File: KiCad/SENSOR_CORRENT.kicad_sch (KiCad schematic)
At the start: 0 parts

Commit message: Actualització del sensor de corrent
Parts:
- added C1: C, symbol Device:C
- added R1: R, symbol Device:R
- added R_Shunt: 10m, symbol Device:R_Shunt
- added U2: INA180A1, Package_TO_SOT_SMD:SOT-23-5, symbol Amplifier_Current:INA180A1
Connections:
- new net: R1.2, U2.1
- new net GND: C1.2, R_Shunt.4, U2.2 (GND)
- new net MOTOR_SENSE_IN: R_Shunt.1
- new net SHUNT_HIGH: R_Shunt.2, U2.3 (+)
- new net SHUNT_LOW: R_Shunt.3, U2.4 (-)
- new net VDD_3V3: U2.5 (V+)
- new net WIN_CURRENT_ADC: C1.1, R1.1

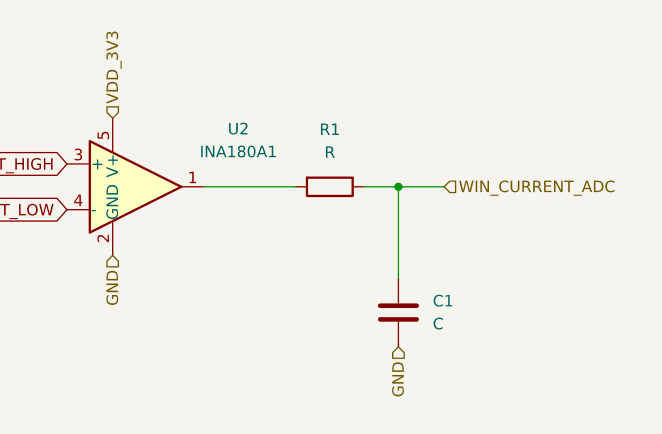
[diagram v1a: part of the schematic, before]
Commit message: Versió amb el simbol del nou micro
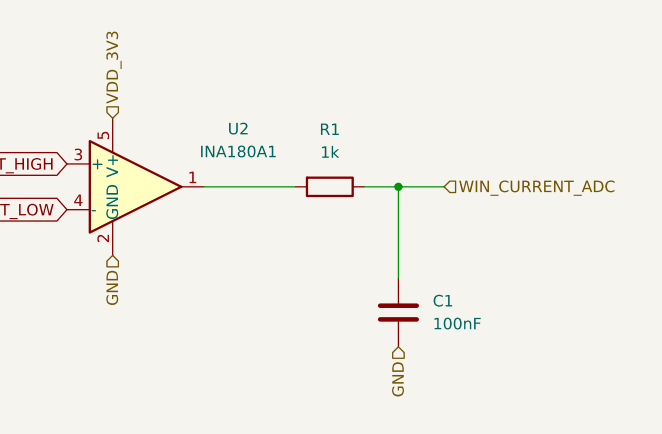
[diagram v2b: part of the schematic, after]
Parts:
- C1: value C -> 100nF
- R1: value R -> 1k
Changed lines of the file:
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@@
 		)
 		(instances
+			(project "SENSOR_CORRENT"
+				(path "/03eea87e-da87-4f21-8136-ad0584e7714c"
+					(reference "R_Shunt1")
+					(unit 1)
+				)
+			)
 			(project ""
 				(path "/347831db-5db9-4aff-ad32-e56fd770e219/0aa311db-868d-4102-819d-96f0255ccb92"
@@
 			)
 		)
-		(property "Value" "R"
+		(property "Value" "1k"
 			(at 132.08 38.1 90)
 			(effects
@@
 		)
 		(instances
+			(project "SENSOR_CORRENT"
+				(path "/03eea87e-da87-4f21-8136-ad0584e7714c"
+					(reference "R1")
+					(unit 1)
+				)
+			)
 			(project ""
 				(path "/347831db-5db9-4aff-ad32-e56fd770e219/0aa311db-868d-4102-819d-96f0255ccb92"
@@
 		)
 		(instances
+			(project "SENSOR_CORRENT"
+				(path "/03eea87e-da87-4f21-8136-ad0584e7714c"
+					(reference "U1")
+					(unit 1)
+				)
+			)
 			(project ""
 				(path "/347831db-5db9-4aff-ad32-e56fd770e219/0aa311db-868d-4102-819d-96f0255ccb92"
@@
 			)
 		)
-		(property "Value" "C"
+		(property "Value" "100nF"
 			(at 143.51 57.1499 0)
 			(effects
@@
 		)
 		(instances
-			(project ""
-				(path "/347831db-5db9-4aff-ad32-e56fd770e219/0aa311db-868d-4102-819d-96f0255ccb92"
+			(project "SENSOR_CORRENT"
+				(path "/03eea87e-da87-4f21-8136-ad0584e7714c"
 					(reference "C1")
 					(unit 1)
 				)
 			)
-		)
-	)
+			(project ""
+				(path "/347831db-5db9-4aff-ad32-e56fd770e219/0aa311db-868d-4102-819d-96f0255ccb92"
+					(reference "C1")
+					(unit 1)
+				)
+			)
+		)
+	)
+	(sheet_instances
+		(path "/"
+			(page "1")
+		)
+	)
+	(embedded_fonts no)
 )

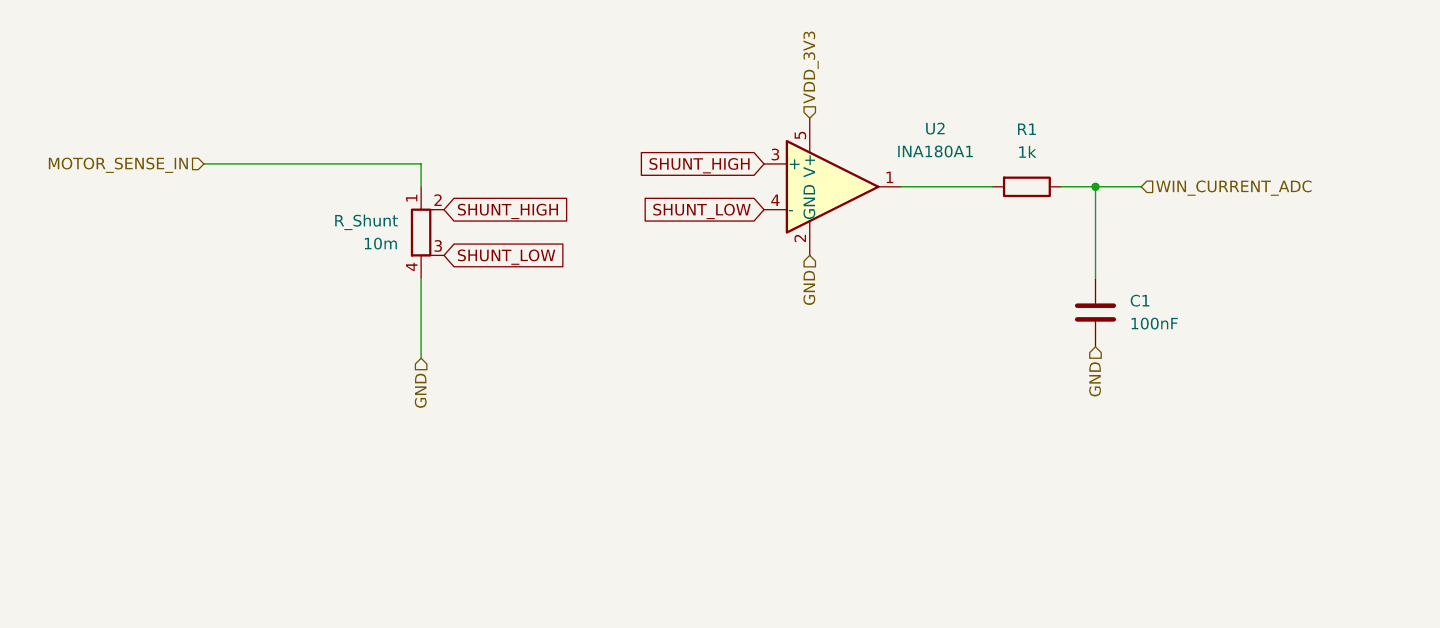
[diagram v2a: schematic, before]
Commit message: Footprints afegides a Comunicació, Sensor RFID i Sensor Corrent
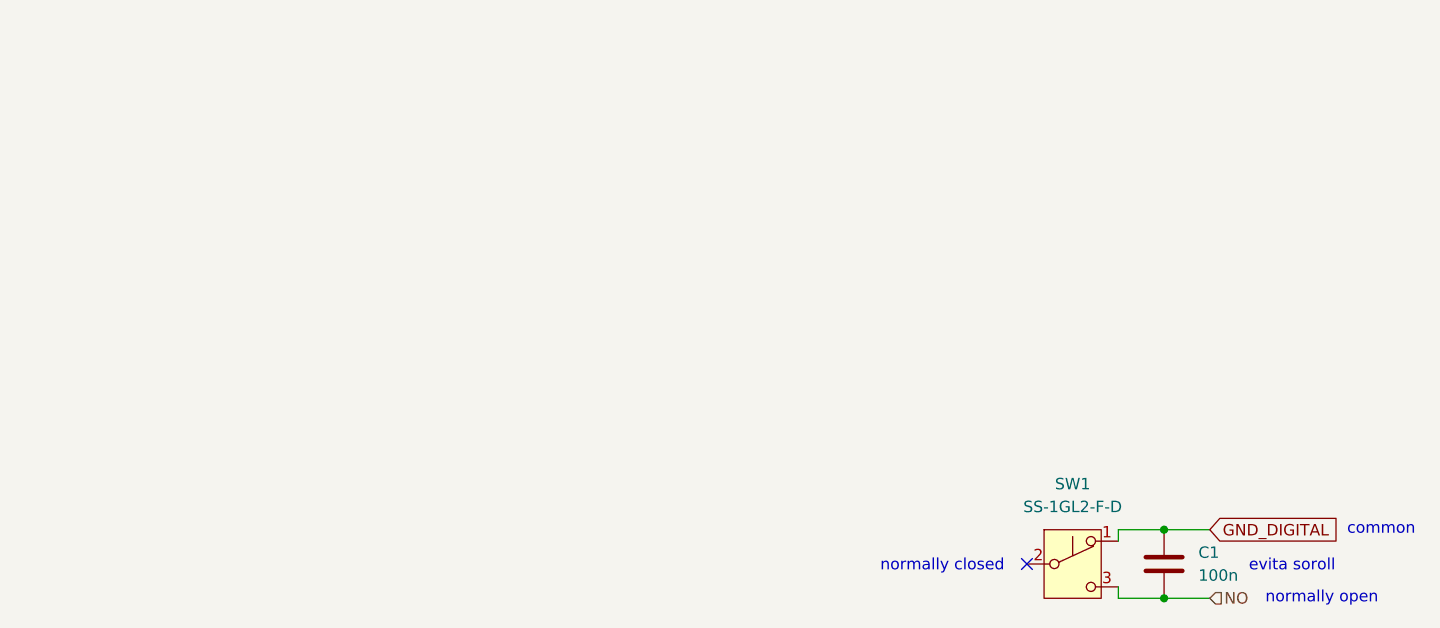
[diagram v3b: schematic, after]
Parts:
- removed R1: 1k, symbol Device:R
- removed R_Shunt: 10m, symbol Device:R_Shunt
- removed U2: INA180A1, Package_TO_SOT_SMD:SOT-23-5, symbol Amplifier_Current:INA180A1
- added SW1: SS-1GL2-F-D, symbol Switch:SW_Push_SPDT
- C1: value 100nF -> 100n; footprint (none) -> Capacitor_SMD:C_0805_2012Metric_Pad1.18x1.45mm_HandSolder
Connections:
- net GND renamed NO
- net NO: now also SW1.3 (NO)
- net WIN_CURRENT_ADC renamed GND_DIGITAL
- net GND_DIGITAL: now also SW1.1 (COM)
- no-connect marks 0 -> 1
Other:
- note added: "common"
- note added: "evita soroll"
- note added: "normally closed"
- note added: "normally open"

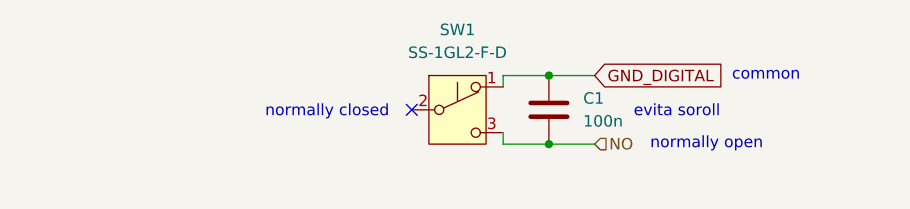
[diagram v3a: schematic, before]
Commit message: Nova versió diagrama de blocs + BOM actualitzat + Nova versió KiCad
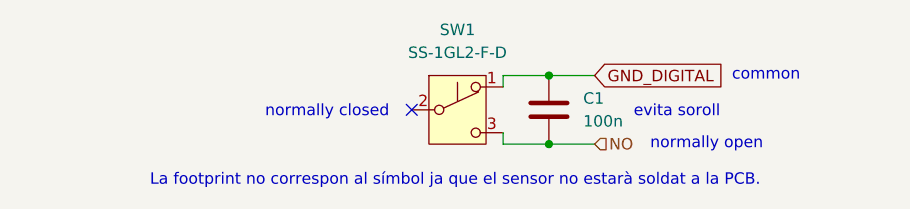
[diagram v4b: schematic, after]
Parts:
- SW1: footprint (none) -> Connector_PinSocket_1.00mm:PinSocket_1x03_P1.00mm_Vertical
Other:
- note added: "La footprint no correspon al símbol ja que el sensor no estarà soldat a la PCB."
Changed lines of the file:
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@@
+		)
+	)
+	(text "La footprint no correspon al símbol ja que el sensor no estarà soldat a la PCB."
+		(exclude_from_sim no)
+		(at 136.906 91.694 0)
+		(effects
+			(font
+				(size 1.27 1.27)
+			)
 		)
 	)
@@
 			)
 		)
-		(property "Footprint" ""
+		(property "Footprint" "Connector_PinSocket_1.00mm:PinSocket_1x03_P1.00mm_Vertical"
 			(at 137.16 83.82 0)
 			(effects

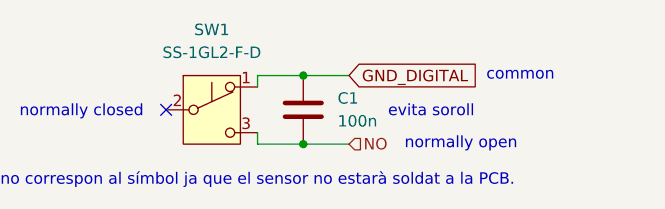
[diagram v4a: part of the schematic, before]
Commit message: Etiquetes de GND i VCC 3.3V canviades a simbols
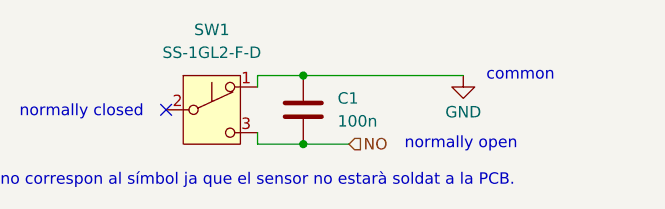
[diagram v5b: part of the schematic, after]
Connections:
- net GND_DIGITAL renamed GND
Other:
- note removed: "evita soroll"
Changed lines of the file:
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@@
-		)
-	)
-	(text "evita soroll"
-		(exclude_from_sim no)
-		(at 161.544 84.074 0)
-		(effects
-			(font
-				(size 1.27 1.27)
-			)
 		)
 	)
@@
 	(wire
 		(pts
-			(xy 147.32 80.01) (xy 152.4 80.01)
-		)
-		(stroke
-			(width 0)
-			(type default)
-		)
-	)
-	(global_label "GND_DIGITAL"
-		(shape input)
-		(at 152.4 80.01 0)
-		(fields_autoplaced yes)
-		(effects
-			(font
-				(size 1.27 1.27)
-			)
-			(justify left)
-		)
-		(property "Intersheetrefs" "${INTERSHEET_REFS}"
-			(at 167.0572 80.01 0)
-			(effects
-				(font
-					(size 1.27 1.27)
-				)
-				(justify left)
-				(hide yes)
-			)
+			(xy 147.32 80.01) (xy 165.1 80.01)
+		)
+		(stroke
+			(width 0)
+			(type default)
 		)
 	)
@@
 					(unit 1)
 				)
+			)
+		)
+	)
+	(symbol
+		(lib_id "power:GND")
+		(at 165.1 80.01 0)
+		(unit 1)
+		(exclude_from_sim no)
+		(in_bom yes)
+		(on_board yes)
+		(dnp no)
+		(property "Reference" "#PWR019"
+			(at 165.1 86.36 0)
+			(effects
+				(font
+					(size 1.27 1.27)
+				)
+				(hide yes)
+			)
+		)
+		(property "Value" "GND"
+			(at 165.1 84.074 0)
+			(effects
+				(font
+					(size 1.27 1.27)
+				)
+			)
+		)
+		(property "Footprint" ""
+			(at 165.1 80.01 0)
+			(effects
+				(font
+					(size 1.27 1.27)
+				)
+				(hide yes)
+			)
+		)
+		(property "Datasheet" ""
+			(at 165.1 80.01 0)
+			(effects
+				(font
+					(size 1.27 1.27)
+				)
+				(hide yes)
+			)
+		)
+		(property "Description" "Power symbol creates a global label with name \"GND\" , ground"
+			(at 165.1 80.01 0)
+			(effects
+				(font
+					(size 1.27 1.27)
+				)
+				(hide yes)
+			)
+		)
+		(pin "1"
+		)
+		(instances
+			(project ""
+				(path "/347831db-5db9-4aff-ad32-e56fd770e219/0aa311db-868d-4102-819d-96f0255ccb92"
+					(reference "#PWR019")
+					(unit 1)
+				)

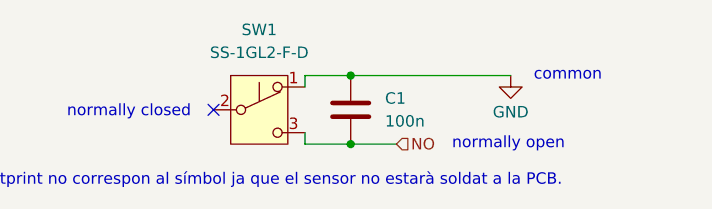
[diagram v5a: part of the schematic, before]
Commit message: Correció etapa d'alimentació e Inputs
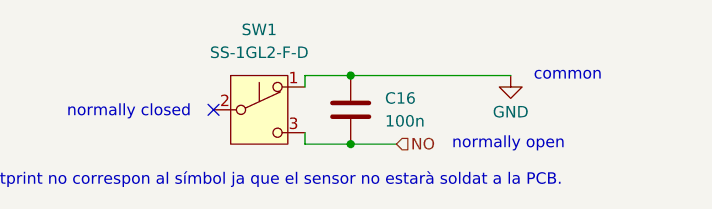
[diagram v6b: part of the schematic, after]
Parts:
- renumbered C1 to C16
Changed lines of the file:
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@@
 		(on_board yes)
 		(dnp no)
-		(property "Reference" "#PWR019"
+		(property "Reference" "#PWR044"
 			(at 165.1 86.36 0)
 			(effects
@@
 			(project ""
 				(path "/347831db-5db9-4aff-ad32-e56fd770e219/0aa311db-868d-4102-819d-96f0255ccb92"
-					(reference "#PWR019")
+					(reference "#PWR044")
 					(unit 1)
 				)
@@
 		(dnp no)
 		(fields_autoplaced yes)
-		(property "Reference" "C1"
+		(property "Reference" "C16"
 			(at 151.13 82.5499 0)
 			(effects
@@
 			(project ""
 				(path "/347831db-5db9-4aff-ad32-e56fd770e219/0aa311db-868d-4102-819d-96f0255ccb92"
-					(reference "C1")
+					(reference "C16")
 					(unit 1)
 				)

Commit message: Versió final Esquematic
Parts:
- added C1: 100n, Capacitor_SMD:C_0805_2012Metric, symbol Device:C
- added J1: Conn_01x08_Pin, Connector_PinSocket_1.00mm:PinSocket_1x08_P1.00mm_Vertical, symbol Connector:Conn_01x08_Pin
- C16: footprint Capacitor_SMD:C_0805_2012Metric_Pad1.18x1.45mm_HandSolder -> Capacitor_SMD:C_0805_2012Metric
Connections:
- net GND: now also C1.2
- net NO renamed WIN_CURRENT_ADC
- new net: C1.1, J1.8 (3.3V)
- new net +3.3V: J1.6 (GND)
- new net RFID_CS: J1.1 (SDA)
- new net RFID_MISO: J1.4 (MISO)
- new net RFID_MOSI: J1.3 (MOSI)
- new net RFID_RST: J1.5 (IRQ)
- new net RFID_SCK: J1.2 (SCK)
- no-connect marks 1 -> 2
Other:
- note added: "decoupling capacitor"
- note added: "master in"
- note added: "master out"
- note added: "reset"
- note added: "serial clock"
- note added: "slave select"

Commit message: Versió final de l'esquematic
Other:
- note added: "REFERENCIA DE COM ES VEU UN SENSOR AL QUAL CONECTAREM A LA PCB"
- note added: "SENSOR FINAL DE CARRERA"
- note added: "SENSOR RFID"
- moved on the sheet: C1, C16, J1, SW1
